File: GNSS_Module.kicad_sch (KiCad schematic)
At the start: 29 parts, among them J301 GPS_Conn, J302 GPS_Conn, J303 GNSS_FTDI_CONN, U301 SAM-M8Q

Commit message: change 10u cap from 0805 to 0402
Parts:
- C303, C304: footprint Capacitor_SMD:C_0805_2012Metric_Pad1.18x1.45mm_HandSolder -> Capacitor_SMD:C_0402_1005Metric; MPN C0805C106K9PACTU -> GRM155R60J106ME05D; Mfr. KEMET -> Murata
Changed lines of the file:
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@@
       (effects (font (size 1.27 1.27)) (justify left))
     )
-    (property "Footprint" "Capacitor_SMD:C_0805_2012Metric_Pad1.18x1.45mm_HandSolder" (at 52.07 30.48 0)
+    (property "Footprint" "Capacitor_SMD:C_0402_1005Metric" (at 52.07 30.48 0)
       (effects (font (size 1.27 1.27)) hide)
     )
@@
       (effects (font (size 1.27 1.27)) (justify left))
     )
-    (property "MPN" "C0805C106K9PACTU" (at 52.07 30.48 0)
+    (property "MPN" "GRM155R60J106ME05D" (at 52.07 30.48 0)
       (effects (font (size 1.27 1.27)) hide)
     )
-    (property "Mfr." "KEMET" (at 52.07 30.48 0)
+    (property "Mfr." "Murata" (at 52.07 30.48 0)
       (effects (font (size 1.27 1.27)) hide)
     )
@@
       (effects (font (size 1.27 1.27)) (justify left))
     )
-    (property "Footprint" "Capacitor_SMD:C_0805_2012Metric_Pad1.18x1.45mm_HandSolder" (at 59.69 30.48 0)
+    (property "Footprint" "Capacitor_SMD:C_0402_1005Metric" (at 59.69 30.48 0)
       (effects (font (size 1.27 1.27)) hide)
     )
@@
       (effects (font (size 1.27 1.27)) (justify left))
     )
-    (property "MPN" "C0805C106K9PACTU" (at 59.69 30.48 0)
+    (property "MPN" "GRM155R60J106ME05D" (at 59.69 30.48 0)
       (effects (font (size 1.27 1.27)) hide)
     )
-    (property "Mfr." "KEMET" (at 59.69 30.48 0)
+    (property "Mfr." "Murata" (at 59.69 30.48 0)
       (effects (font (size 1.27 1.27)) hide)
     )

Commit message: replace passives with 0402
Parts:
- C301, C302, C305: footprint Capacitor_SMD:C_0603_1608Metric_Pad1.08x0.95mm_HandSolder -> Capacitor_SMD:C_0402_1005Metric; MPN C0603C105K8RACTU -> C0402C105K9PACTU
- FB904: footprint Inductor_SMD:L_0603_1608Metric_Pad1.05x0.95mm_HandSolder -> Inductor_SMD:L_0402_1005Metric; MPN BLM18KG101TZ1D -> BLM15HD102SN1D
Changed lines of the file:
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@@
       (effects (font (size 1.27 1.27)) (justify left))
     )
-    (property "Footprint" "Capacitor_SMD:C_0603_1608Metric_Pad1.08x0.95mm_HandSolder" (at 78.74 30.48 0)
+    (property "Footprint" "Capacitor_SMD:C_0402_1005Metric" (at 78.74 30.48 0)
       (effects (font (size 1.27 1.27)) hide)
     )
@@
       (effects (font (size 1.27 1.27)) hide)
     )
-    (property "MPN" "C0603C105K8RACTU" (at 78.74 30.48 0)
+    (property "MPN" "C0402C105K9PACTU" (at 78.74 30.48 0)
       (effects (font (size 1.27 1.27)) hide)
     )
@@
       (effects (font (size 1.27 1.27)) hide)
     )
-    (property "Footprint" "Inductor_SMD:L_0603_1608Metric_Pad1.05x0.95mm_HandSolder" (at 27.94 57.023 90)
+    (property "Footprint" "Inductor_SMD:L_0402_1005Metric" (at 27.94 57.023 90)
       (effects (font (size 1.27 1.27)) hide)
     )
@@
       (effects (font (size 1.27 1.27)) hide)
     )
-    (property "MPN" "BLM18KG101TZ1D" (at 27.94 55.245 90)
+    (property "MPN" "BLM15HD102SN1D" (at 27.94 55.245 90)
       (effects (font (size 1.27 1.27)) hide)
     )
@@
       (effects (font (size 1.27 1.27)) (justify left))
     )
-    (property "Footprint" "Capacitor_SMD:C_0603_1608Metric_Pad1.08x0.95mm_HandSolder" (at 36.83 61.595 0)
+    (property "Footprint" "Capacitor_SMD:C_0402_1005Metric" (at 36.83 61.595 0)
       (effects (font (size 1.27 1.27)) hide)
     )
@@
       (effects (font (size 1.27 1.27)) hide)
     )
-    (property "MPN" "C0603C105K8RACTU" (at 36.83 61.595 0)
+    (property "MPN" "C0402C105K9PACTU" (at 36.83 61.595 0)
       (effects (font (size 1.27 1.27)) hide)
     )
@@
       (effects (font (size 1.27 1.27)) (justify left))
     )
-    (property "Footprint" "Capacitor_SMD:C_0603_1608Metric_Pad1.08x0.95mm_HandSolder" (at 21.59 61.595 0)
+    (property "Footprint" "Capacitor_SMD:C_0402_1005Metric" (at 21.59 61.595 0)
       (effects (font (size 1.27 1.27)) hide)
     )
@@
       (effects (font (size 1.27 1.27)) hide)
     )
-    (property "MPN" "C0603C105K8RACTU" (at 21.59 61.595 0)
-      (effects (font (size 1.27 1.27)) hide)
-    )
+    (property "MPN" "C0402C105K9PACTU" (at 21.59 61.595 0)
+      (effects (font (size 1.27 1.27)) hide)
+    )

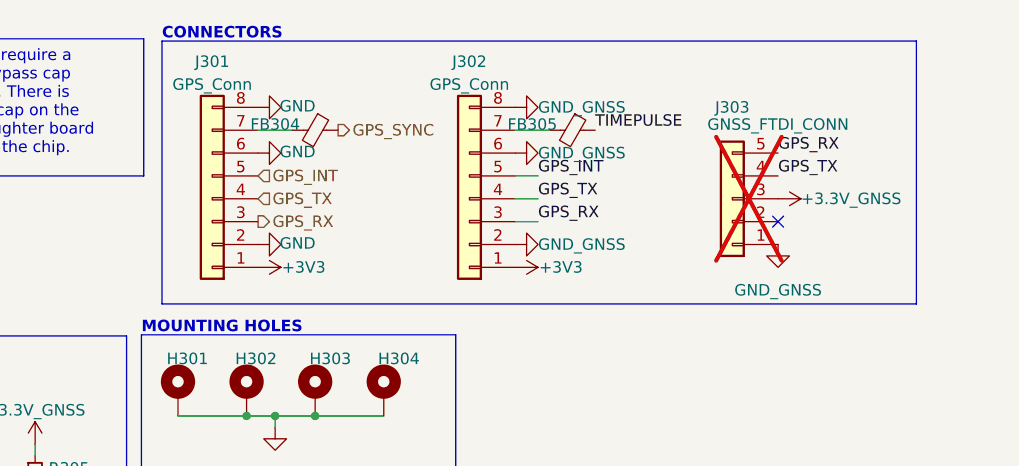
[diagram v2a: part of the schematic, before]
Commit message: (pcb) route power
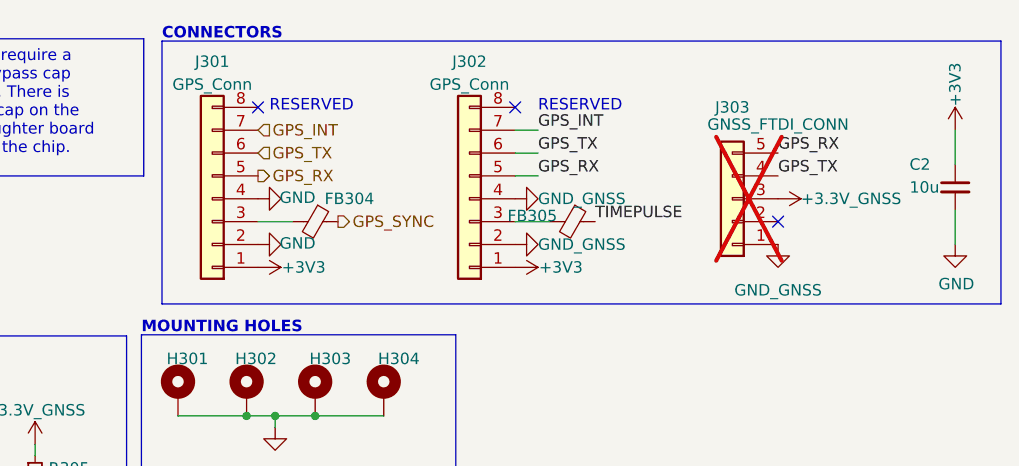
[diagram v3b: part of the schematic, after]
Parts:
- added C2: 10u, Capacitor_SMD:C_0402_1005Metric, symbol Device:C_Small
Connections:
- net +3V3: now also C2.1
- net GND: now also J301.4 (Pin_4), J302.4 (Pin_4), C2.2; no longer J301.6 (Pin_6), J301.8 (Pin_8), J302.6 (Pin_6), J302.8 (Pin_8)
- net GPS_INT: now also J301.7 (Pin_7), J302.7 (Pin_7); no longer J301.5 (Pin_5), J302.5 (Pin_5)
- net GPS_RX: now also J301.5 (Pin_5), J302.5 (Pin_5); no longer J301.3 (Pin_3), J302.3 (Pin_3)
- net GPS_TX: now also J301.6 (Pin_6), J302.6 (Pin_6); no longer J301.4 (Pin_4), J302.4 (Pin_4)
- net at FB305.2: now also J302.3 (Pin_3); no longer J302.7 (Pin_7)
- net at FB304.2: now also J301.3 (Pin_3); no longer J301.7 (Pin_7)
- no-connect marks 4 -> 6
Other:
- note added: "RESERVED"
- moved on the sheet: FB304, FB305

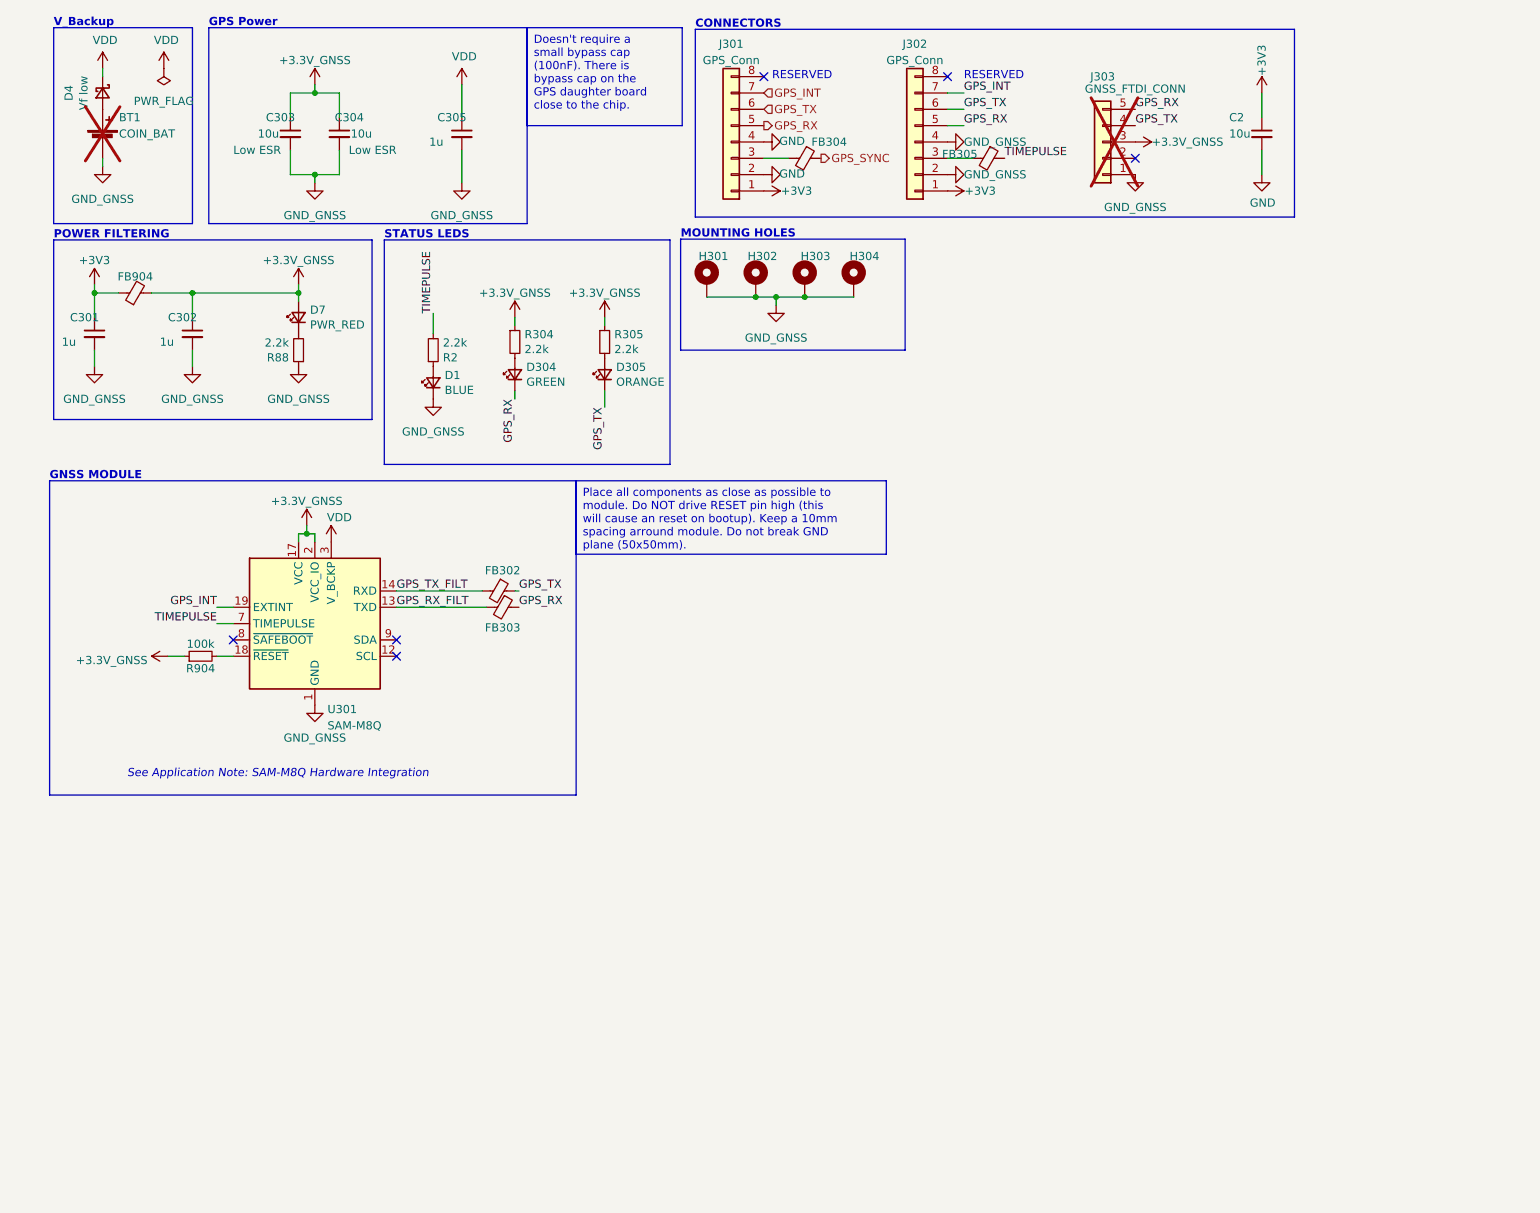
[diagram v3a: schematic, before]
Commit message: (sch) fix board seperate net labels
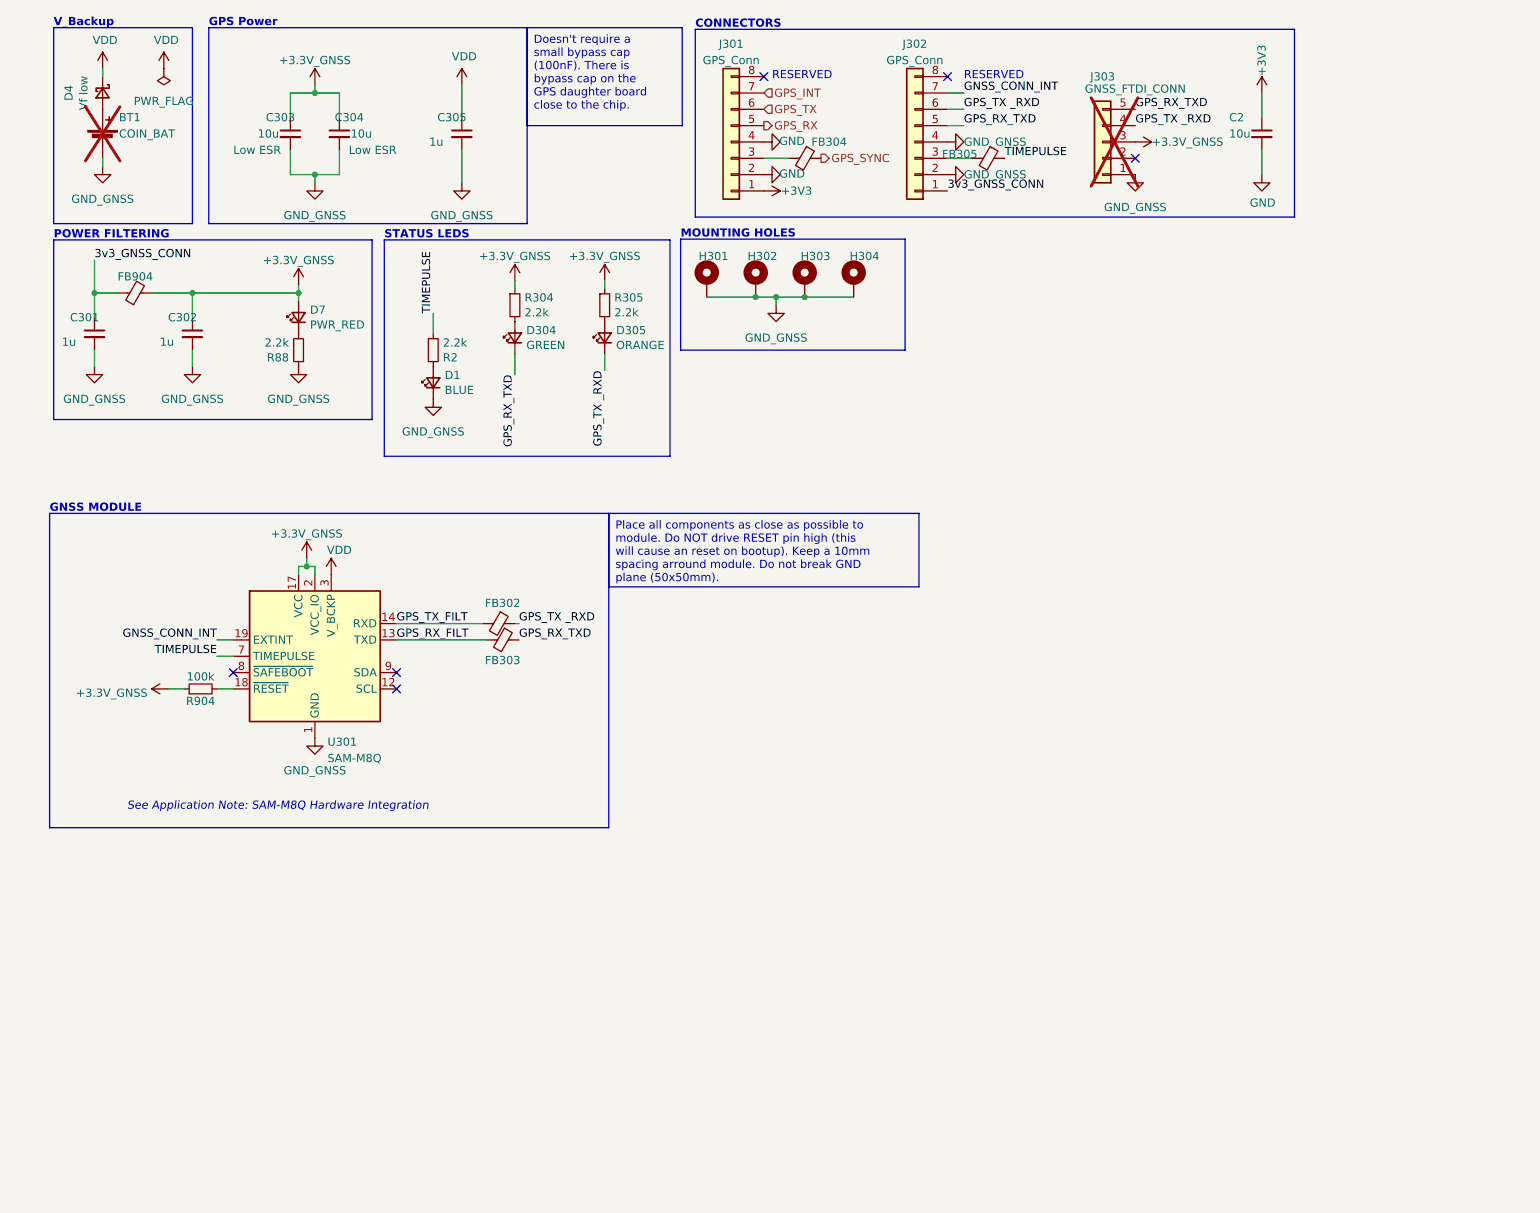
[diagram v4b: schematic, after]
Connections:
- net +3V3: no longer C301.1, FB904.1, J302.1 (Pin_1)
- net GND: no longer BT1.2 (-), C301.2, C302.2, C303.2, C304.2, C305.2, D1.1 (K), H301.1, H302.1, H303.1, H304.1, J302.2 (Pin_2), J302.4 (Pin_4), J303.1 (Pin_1), R88.1, U301.1 (GND), U301.10 (GND), U301.11 (GND), U301.15 (GND), U301.16 (GND), U301.20 (GND), U301.4 (GND), U301.5 (GND), U301.6 (GND)
- net GPS_INT: no longer J302.7 (Pin_7), U301.19 (EXTINT)
- net GPS_RX: no longer D304.1 (K), FB303.1, J302.5 (Pin_5), J303.5 (Pin_5)
- net GPS_TX: no longer D305.1 (K), FB302.1, J302.6 (Pin_6), J303.4 (Pin_4)
- net +3.3V renamed +3.3V_GNSS
- new net 3v3_GNSS_CONN: C301.1, FB904.1, J302.1 (Pin_1)
- new net GND_GNSS: BT1.2 (-), C301.2, C302.2, C303.2, C304.2, C305.2, D1.1 (K), H301.1, H302.1, H303.1, H304.1, J302.2 (Pin_2), J302.4 (Pin_4), J303.1 (Pin_1), R88.1, U301.1 (GND), U301.10 (GND), U301.11 (GND), U301.15 (GND), U301.16 (GND), U301.20 (GND), U301.4 (GND), U301.5 (GND), U301.6 (GND)
- new net GNSS_CONN_INT: J302.7 (Pin_7), U301.19 (EXTINT)
- new net GPS_RX_TXD: D304.1 (K), FB303.1, J302.5 (Pin_5), J303.5 (Pin_5)
- new net GPS_TX _RXD: D305.1 (K), FB302.1, J302.6 (Pin_6), J303.4 (Pin_4)
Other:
- moved on the sheet: D304, D305, FB302, FB303, R304, R305, R904, U301

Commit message: (pcb) GNSS board layout
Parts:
- D4: footprint Diode_SMD:D_SOD-123 -> Diode_SMD:D_SOD-523; MPN RSX101MM-30TR -> RB520S30T1G; Mfr. ROHM Semiconductor -> onsemi
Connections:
- net GPS_TX _RXD: no longer FB302.1, J302.6 (Pin_6)
- net GPS_RX_FILT renamed GNSS_TXD
- net GPS_TX_FILT renamed GNSS_RXD
- new net GPS_TX_RXD: FB302.1, J302.6 (Pin_6)
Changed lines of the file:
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@@
     (effects (font (size 1.27 1.27)) (justify right bottom))
   )
-  (label "GPS_TX _RXD" (at 156.845 26.67 0) (fields_autoplaced)
+  (label "GPS_TX_RXD" (at 156.845 26.67 0) (fields_autoplaced)
     (effects (font (size 1.27 1.27)) (justify left bottom))
   )
@@
     (effects (font (size 1.27 1.27)) (justify right bottom))
   )
-  (label "GPS_TX _RXD" (at 87.63 106.68 0) (fields_autoplaced)
+  (label "GPS_TX_RXD" (at 87.63 106.68 0) (fields_autoplaced)
     (effects (font (size 1.27 1.27)) (justify left bottom))
   )
@@
     (effects (font (size 1.27 1.27)) (justify left bottom))
   )
-  (label "GPS_TX_FILT" (at 68.58 106.68 0) (fields_autoplaced)
+  (label "GNSS_RXD" (at 68.58 106.68 0) (fields_autoplaced)
     (effects (font (size 1.27 1.27)) (justify left bottom))
   )
@@
     (effects (font (size 1.27 1.27)) (justify left bottom))
   )
-  (label "GPS_RX_FILT" (at 68.58 109.22 0) (fields_autoplaced)
+  (label "GNSS_TXD" (at 68.58 109.22 0) (fields_autoplaced)
     (effects (font (size 1.27 1.27)) (justify left bottom))
   )
@@
       (effects (font (size 1.27 1.27)))
     )
-    (property "Footprint" "Diode_SMD:D_SOD-123" (at 22.86 24.13 90)
+    (property "Footprint" "Diode_SMD:D_SOD-523" (at 22.86 24.13 90)
       (effects (font (size 1.27 1.27)) hide)
     )
@@
       (effects (font (size 1.27 1.27)) hide)
     )
-    (property "MPN" "RSX101MM-30TR" (at 22.86 24.13 0)
-      (effects (font (size 1.27 1.27)) hide)
-    )
-    (property "Mfr." "ROHM Semiconductor" (at 22.86 24.13 0)
-      (effects (font (size 1.27 1.27)) hide)
-    )
+    (property "MPN" "RB520S30T1G" (at 22.86 24.13 0)
+      (effects (font (size 1.27 1.27)) hide)
+    )
+    (property "Mfr." "onsemi" (at 22.86 24.13 0)
+      (effects (font (size 1.27 1.27)) hide)
+    )

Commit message: (pcb) finalise GNSS board
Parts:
- removed R904: 100k, Resistor_SMD:R_0402_1005Metric, symbol Device:R_Small
- added JP1: GNSS_CONN_~{RESET}_SEL, Jumper:SolderJumper-2_P1.3mm_Open_RoundedPad1.0x1.5mm, symbol Jumper:SolderJumper_2_Open
- added JP2: GNSS_CONN_EXT_INT_SEL, Jumper:SolderJumper-2_P1.3mm_Open_RoundedPad1.0x1.5mm, symbol Jumper:SolderJumper_2_Open
- J301: value GPS_Conn -> GNSS_MAINBOARD_CONN
- J302: value GPS_Conn -> GNSS_MODULE_BOARD_CONNECTOR
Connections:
- net GPS_INT is gone; now on net GPS_RX: J301.7 (Pin_7)
- net GPS_TX _RXD is gone; now on net GPS_TX_RXD: D305.1 (K), J303.4 (Pin_4)
- net +3.3V_GNSS: now also R2.2
- net GND: now also J301.6 (Pin_6); no longer J301.4 (Pin_4)
- net GND_GNSS: now also J302.6 (Pin_6); no longer D1.1 (K), J302.4 (Pin_4)
- net GNSS_CONN_INT: now also J302.3 (Pin_3), JP2.1 (A); no longer J302.7 (Pin_7), U301.19 (EXTINT)
- net GPS_RX: no longer J301.5 (Pin_5)
- net GPS_RX_TXD: now also J302.7 (Pin_7); no longer J302.5 (Pin_5)
- net GPS_TX: now also J301.8 (Pin_8); no longer J301.6 (Pin_6)
- net GPS_TX_RXD: now also J302.8 (Pin_8); no longer J302.6 (Pin_6)
- net TIMEPULSE: now also D1.1 (K); no longer R2.2
- net GNSS_~{RESET}: now reaches U301.18 (~{RESET})
- net GNSS_~{RESET}: now also JP1.2 (B)
- net BATT+: now reaches BT1.1 (+), D4.2 (A)
- net at FB305.2: now also J302.5 (Pin_5); no longer J302.3 (Pin_3)
- net at J301.3 (Pin_3): no longer FB304.2
- new net: FB304.2, J301.5 (Pin_5)
- new net GNSS_CONN_~{RESET}: J302.4 (Pin_4), JP1.1 (A)
- new net GNSS_EXT_INT: JP2.2 (B), U301.19 (EXTINT)
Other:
- note added: "[NOT CONNECTED] GNSS_EXT_INT"
- note added: "[NOT CONNECTED] GNSS_~{RESET}"
- note removed: "RESERVED"
- moved on the sheet: BT1, C2, D1, D4, FB304, FB305, J302, J303, R2

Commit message: (sch) run DRC
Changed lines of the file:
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@@
+    )
+  )
+  (symbol (lib_id "power:PWR_FLAG") (at 19.05 189.865 180) (unit 1)
+    (in_bom yes) (on_board yes) (dnp no) (fields_autoplaced)
+    (property "Reference" "#FLG0302" (at 19.05 191.77 0)
+      (effects (font (size 1.27 1.27)) hide)
+    )
+    (property "Value" "PWR_FLAG" (at 19.05 194.945 0)
+      (effects (font (size 1.27 1.27)))
+    )
+    (property "Footprint" "" (at 19.05 189.865 0)
+      (effects (font (size 1.27 1.27)) hide)
+    )
+    (property "Datasheet" "~" (at 19.05 189.865 0)
+      (effects (font (size 1.27 1.27)) hide)
+    )
+    (pin "1")
+    (instances
+      (project "kleinvoet"
+        (path "/4185c36c-c66e-4dbd-be5d-841e551f4885/00000000-0000-0000-0000-00005edf3693"
+          (reference "#FLG0302") (unit 1)
+        )
+      )
     )
   )
@@
     )
   )
+  (symbol (lib_id "grootvoet:+3.3V_GNSS") (at 19.05 189.865 0) (unit 1)
+    (in_bom yes) (on_board yes) (dnp no) (fields_autoplaced)
+    (property "Reference" "#PWR0301" (at 19.05 193.675 0)
+      (effects (font (size 1.27 1.27)) hide)
+    )
+    (property "Value" "+3.3V_GNSS" (at 19.05 186.055 0)
+      (effects (font (size 1.27 1.27)))
+    )
+    (property "Footprint" "" (at 19.05 189.865 0)
+      (effects (font (size 1.27 1.27)) hide)
+    )
+    (property "Datasheet" "" (at 19.05 189.865 0)
+      (effects (font (size 1.27 1.27)) hide)
+    )
+    (pin "1")
+    (instances
+      (project "kleinvoet"
+        (path "/4185c36c-c66e-4dbd-be5d-841e551f4885/00000000-0000-0000-0000-00005edf3693"
+          (reference "#PWR0301") (unit 1)
+        )
+      )
+    )
+  )
   (symbol (lib_id "Connector_Generic:Conn_01x08") (at 120.65 31.75 180) (unit 1)
     (in_bom yes) (on_board yes) (dnp no)
@@
         )
       )
+    )
+  )
+  (symbol (lib_id "grootvoet:GND_GNSS") (at 30.48 189.865 0) (unit 1)
+    (in_bom yes) (on_board yes) (dnp no) (fields_autoplaced)
+    (property "Reference" "#PWR0306" (at 30.48 196.215 0)
+      (effects (font (size 1.27 1.27)) hide)
+    )
+    (property "Value" "GND_GNSS" (at 30.48 194.945 0)
+      (effects (font (size 1.27 1.27)))
+    )
+    (property "Footprint" "" (at 30.48 189.865 0)
+      (effects (font (size 1.27 1.27)) hide)
+    )
+    (property "Datasheet" "" (at 30.48 189.865 0)
+      (effects (font (size 1.27 1.27)) hide)
+    )
+    (pin "1")
+    (instances
+      (project "kleinvoet"
+        (path "/4185c36c-c66e-4dbd-be5d-841e551f4885/00000000-0000-0000-0000-00005edf3693"
+          (reference "#PWR0306") (unit 1)
+        )
+      )
+    )
+  )
+  (symbol (lib_id "power:PWR_FLAG") (at 30.48 189.865 0) (unit 1)
+    (in_bom yes) (on_board yes) (dnp no) (fields_autoplaced)
+    (property "Reference" "#FLG0303" (at 30.48 187.96 0)
+      (effects (font (size 1.27 1.27)) hide)
+    )
+    (property "Value" "PWR_FLAG" (at 30.48 186.69 0)
+      (effects (font (size 1.27 1.27)))
+    )
+    (property "Footprint" "" (at 30.48 189.865 0)
+      (effects (font (size 1.27 1.27)) hide)
+    )
+    (property "Datasheet" "~" (at 30.48 189.865 0)
+      (effects (font (size 1.27 1.27)) hide)
+    )
+    (pin "1")
+    (instances
+      (project "kleinvoet"
+        (path "/4185c36c-c66e-4dbd-be5d-841e551f4885/00000000-0000-0000-0000-00005edf3693"
+          (reference "#FLG0303") (unit 1)
+        )
+      )
